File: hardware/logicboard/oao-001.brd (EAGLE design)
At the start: 47 x 47 mm, 13 parts, among them K1 G5V1, T1 2SC1815

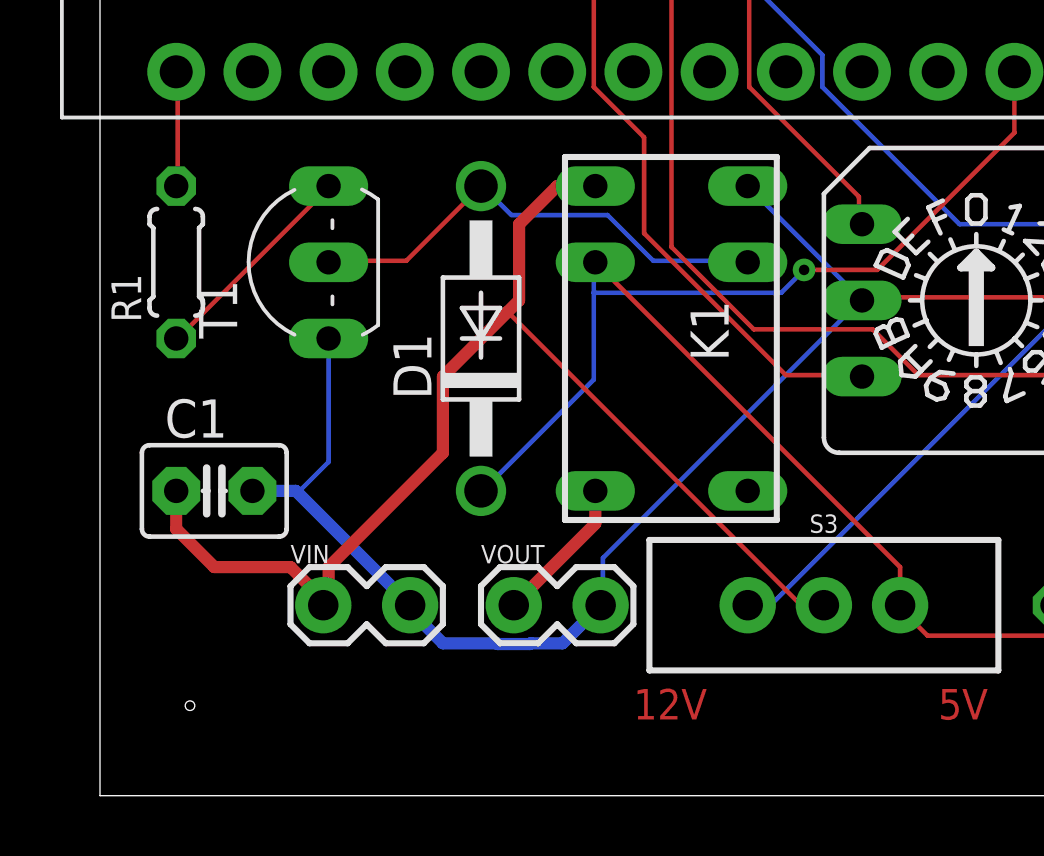
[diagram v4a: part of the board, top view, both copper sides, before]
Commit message: Changed layout.
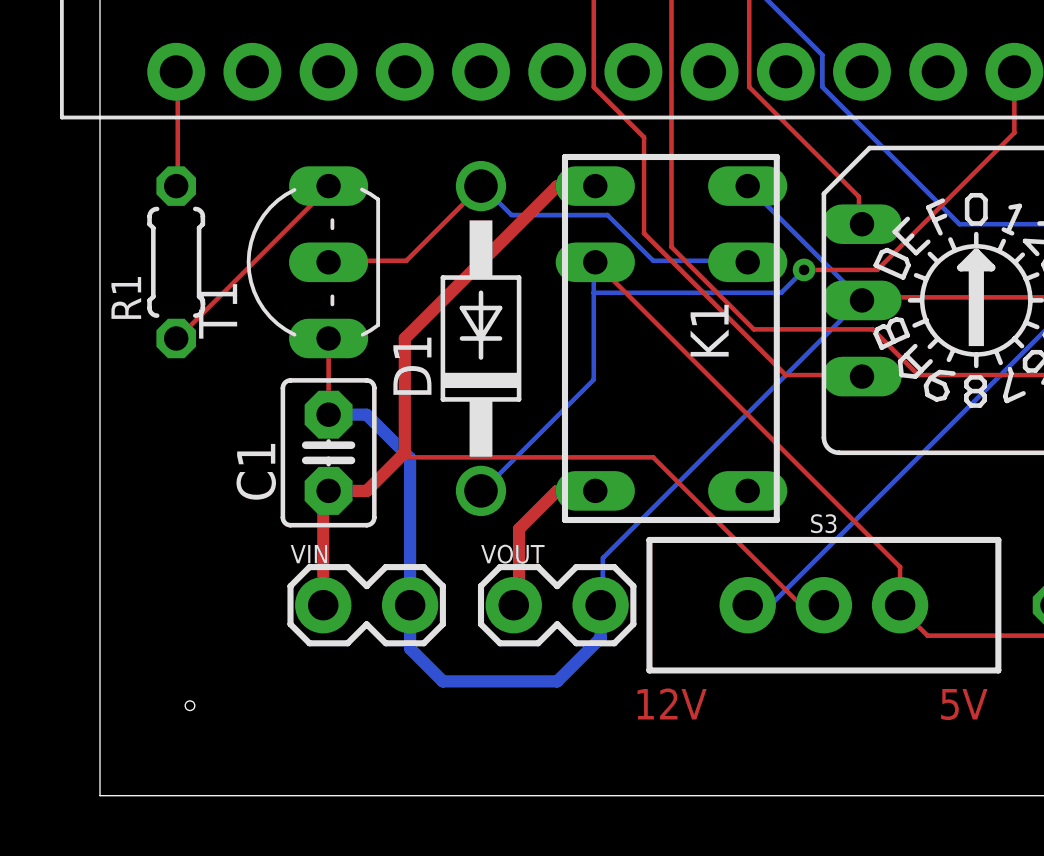
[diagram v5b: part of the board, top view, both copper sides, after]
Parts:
- moved C1 4.02 mm to (7.62, 11.4), turned to 90 degrees
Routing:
- net VDD: track 41.2 -> 35.3 mm
- net GND: track 60.1 -> 60.9 mm
- net N$1: track 4.94 -> 5.68 mm
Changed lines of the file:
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@@
 <attribute name="SF_SKU" value="COM-00102" x="24.13" y="6.35" size="1.778" layer="27" rot="R270" display="off"/>
 </element>
-<element name="C1" library="capacitor-wima" library_urn="urn:adsk.eagle:library:116" package="C2.5-3" package3d_urn="urn:adsk.eagle:package:5436/1" value="" x="3.81" y="10.16"/>
+<element name="C1" library="capacitor-wima" library_urn="urn:adsk.eagle:library:116" package="C2.5-3" package3d_urn="urn:adsk.eagle:package:5436/1" value="" x="7.62" y="11.43" rot="R90"/>
 </elements>
 <signals>
@@
 <contactref element="S3" pad="2"/>
 <contactref element="C1" pad="1"/>
+<wire x1="7.4422" y1="6.35" x2="7.4422" y2="9.9822" width="0.4064" layer="1"/>
+<wire x1="7.4422" y1="9.9822" x2="7.62" y2="10.16" width="0.4064" layer="1"/>
 <wire x1="16.51" y1="20.32" x2="15.24" y2="20.32" width="0.4064" layer="1"/>
-<wire x1="15.24" y1="20.32" x2="13.97" y2="19.05" width="0.4064" layer="1"/>
-<wire x1="13.97" y1="19.05" x2="13.97" y2="16.51" width="0.4064" layer="1"/>
-<wire x1="13.97" y1="16.51" x2="13.589" y2="16.129" width="0.4064" layer="1"/>
-<wire x1="13.589" y1="16.129" x2="11.43" y2="13.97" width="0.4064" layer="1"/>
-<wire x1="11.43" y1="13.97" x2="11.43" y2="11.43" width="0.4064" layer="1"/>
-<wire x1="11.43" y1="11.43" x2="7.62" y2="7.62" width="0.4064" layer="1"/>
-<wire x1="7.62" y1="7.62" x2="7.62" y2="6.5278" width="0.4064" layer="1"/>
-<wire x1="7.4422" y1="6.35" x2="7.62" y2="6.5278" width="0.4064" layer="1"/>
-<wire x1="2.54" y1="10.16" x2="2.54" y2="8.89" width="0.4064" layer="1"/>
-<wire x1="2.54" y1="8.89" x2="3.81" y2="7.62" width="0.4064" layer="1"/>
-<wire x1="3.81" y1="7.62" x2="6.35" y2="7.62" width="0.4064" layer="1"/>
-<wire x1="6.35" y1="7.62" x2="7.4422" y2="6.5278" width="0.4064" layer="1"/>
-<wire x1="7.4422" y1="6.5278" x2="7.4422" y2="6.35" width="0.4064" layer="1"/>
+<wire x1="15.24" y1="20.32" x2="10.16" y2="15.24" width="0.4064" layer="1"/>
+<wire x1="10.16" y1="15.24" x2="10.16" y2="11.43" width="0.4064" layer="1"/>
+<wire x1="10.16" y1="11.43" x2="10.1092" y2="11.3792" width="0.4064" layer="1"/>
+<wire x1="10.1092" y1="11.3792" x2="8.89" y2="10.16" width="0.4064" layer="1"/>
+<wire x1="8.89" y1="10.16" x2="7.62" y2="10.16" width="0.4064" layer="1"/>
 <wire x1="23.3172" y1="6.4008" x2="24.0792" y2="6.4008" width="0.1524" layer="1"/>
+<wire x1="18.4404" y1="11.2776" x2="23.3172" y2="6.4008" width="0.1524" layer="1"/>
+<wire x1="10.2108" y1="11.2776" x2="18.4404" y2="11.2776" width="0.1524" layer="1"/>
 <wire x1="24.0792" y1="6.4008" x2="24.13" y2="6.35" width="0.1524" layer="1"/>
-<wire x1="13.589" y1="16.129" x2="23.3172" y2="6.4008" width="0.1524" layer="1"/>
-<wire x1="23.3172" y1="6.4008" x2="24.13" y2="6.35" width="0.1524" layer="1"/>
+<wire x1="10.2108" y1="11.2776" x2="10.1092" y2="11.3792" width="0.1524" layer="1"/>
 </signal>
 <signal name="GND">
@@
 <contactref element="VIN" pad="2"/>
 <contactref element="C1" pad="2"/>
-<wire x1="16.6878" y1="6.35" x2="15.4178" y2="5.08" width="0.4064" layer="16"/>
-<wire x1="14.354175" y1="5.08" x2="14.328775" y2="5.0546" width="0.4064" layer="16"/>
-<wire x1="14.328775" y1="5.0546" x2="13.255625" y2="5.0546" width="0.4064" layer="16"/>
-<wire x1="13.255625" y1="5.0546" x2="13.230225" y2="5.08" width="0.4064" layer="16"/>
-<wire x1="13.230225" y1="5.08" x2="11.43" y2="5.08" width="0.4064" layer="16"/>
-<wire x1="15.4178" y1="5.08" x2="14.354175" y2="5.08" width="0.4064" layer="16"/>
-<wire x1="11.43" y1="5.08" x2="10.3378" y2="6.1722" width="0.4064" layer="16"/>
-<wire x1="10.3378" y1="6.1722" x2="10.3378" y2="6.35" width="0.4064" layer="16"/>
-<wire x1="10.3378" y1="6.35" x2="6.5278" y2="10.16" width="0.4064" layer="16"/>
-<wire x1="6.5278" y1="10.16" x2="5.08" y2="10.16" width="0.4064" layer="16"/>
+<wire x1="10.3378" y1="6.35" x2="10.3378" y2="4.9022" width="0.4064" layer="16"/>
+<wire x1="10.3378" y1="4.9022" x2="11.43" y2="3.81" width="0.4064" layer="16"/>
+<wire x1="11.43" y1="3.81" x2="15.24" y2="3.81" width="0.4064" layer="16"/>
+<wire x1="16.6878" y1="5.2578" x2="16.6878" y2="6.35" width="0.4064" layer="16"/>
+<wire x1="15.24" y1="3.81" x2="16.6878" y2="5.2578" width="0.4064" layer="16"/>
+<wire x1="7.62" y1="12.7" x2="8.89" y2="12.7" width="0.4064" layer="16"/>
+<wire x1="10.3378" y1="11.2522" x2="10.3378" y2="6.35" width="0.4064" layer="16"/>
+<wire x1="8.89" y1="12.7" x2="10.3378" y2="11.2522" width="0.4064" layer="16"/>
 <wire x1="36.8808" y1="17.0688" x2="36.8808" y2="16.6116" width="0.1524" layer="1"/>
 <wire x1="38.4048" y1="18.5928" x2="36.8808" y2="17.0688" width="0.1524" layer="1"/>
@@
 <wire x1="36.8808" y1="16.6116" x2="36.83" y2="16.51" width="0.1524" layer="1"/>
 <wire x1="35.6616" y1="24.0792" x2="35.56" y2="24.13" width="0.1524" layer="1"/>
-<wire x1="7.62" y1="11.1252" x2="7.62" y2="15.24" width="0.1524" layer="16"/>
-<wire x1="6.7056" y1="10.2108" x2="7.62" y2="11.1252" width="0.1524" layer="16"/>
-<wire x1="6.7056" y1="10.2108" x2="6.5278" y2="10.16" width="0.1524" layer="16"/>
-<wire x1="25.4" y1="16.51" x2="21.59" y2="20.32" width="0.1524" layer="16"/>
+<wire x1="7.62" y1="12.7" x2="7.62" y2="15.24" width="0.1524" layer="1"/>
+<wire x1="21.59" y1="20.32" x2="25.4" y2="16.51" width="0.1524" layer="16"/>
 <wire x1="16.764" y1="7.9248" x2="16.764" y2="6.4008" width="0.1524" layer="16"/>
 <wire x1="25.2984" y1="16.4592" x2="16.764" y2="7.9248" width="0.1524" layer="16"/>
@@
 <contactref element="K1" pad="5"/>
 <contactref element="VOUT" pad="1"/>
-<wire x1="13.7922" y1="6.35" x2="16.51" y2="9.0678" width="0.4064" layer="1"/>
-<wire x1="16.51" y1="9.0678" x2="16.51" y2="10.16" width="0.4064" layer="1"/>
+<wire x1="16.51" y1="10.16" x2="15.24" y2="10.16" width="0.4064" layer="1"/>
+<wire x1="15.24" y1="10.16" x2="13.97" y2="8.89" width="0.4064" layer="1"/>
+<wire x1="13.97" y1="8.89" x2="13.97" y2="6.5278" width="0.4064" layer="1"/>
+<wire x1="13.97" y1="6.5278" x2="13.7922" y2="6.35" width="0.4064" layer="1"/>
 </signal>
 <signal name="N$2">
@@
 <contactref element="R2" pad="1"/>
 <wire x1="31.8516" y1="7.0104" x2="31.8516" y2="6.4008" width="0.1524" layer="16"/>
-<wire x1="31.8516" y1="6.4008" x2="31.75" y2="6.35" width="0.1524" layer="16"/>
 <wire x1="39.3192" y1="14.478" x2="31.8516" y2="7.0104" width="0.1524" layer="16"/>
 <wire x1="39.3192" y1="28.0416" x2="39.3192" y2="14.478" width="0.1524" layer="16"/>
 <wire x1="28.0416" y1="39.3192" x2="39.3192" y2="28.0416" width="0.1524" layer="16"/>
+<wire x1="31.8516" y1="6.4008" x2="31.75" y2="6.35" width="0.1524" layer="16"/>
 <wire x1="28.0416" y1="39.3192" x2="27.94" y2="39.37" width="0.1524" layer="16"/>
 </signal>

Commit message: GND.
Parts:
- VOLTAGE-SELECT: value NC: 5V, NO: 12V -> 12V-5V
- moved D1 1.27 mm to (12.7, 16.5)
- moved VOUT 1.27 mm to (12.7, 6.35)
- moved C1 1.27 mm to (7.62, 12.7)
- moved R1 1.27 mm to (2.54, 19.1)
- moved T1 1.27 mm to (7.62, 19.1)
- renumbered D2 to LED, K1 to RELAY, S1 to ON-INT, S2 to OFF-INT, S3 to VOLTAGE-SELECT
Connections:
- net N$13 renamed LEDDRIVE
- net N$15 renamed V12
- net N$2 renamed RELAYDRIVE
- removed net N$12: OFF-INT.1, U$1.P$9
- new net N$2: OFF-INT.8, U$1.P$5
- net N$11: now also OFF-INT.1; no longer OFF-INT.2
- net N$5: now also OFF-INT.4; no longer OFF-INT.8
- net N$6: now also OFF-INT.2; no longer OFF-INT.4
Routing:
- net N$2: track 0.00 -> 45.4 mm
- net N$12: track 26.2 -> 0.00 mm
- net N$11: track 42.0 -> 31.8 mm
- net N$9: track 41.6 -> 50.3 mm
- net LEDDRIVE: track 40.9 -> 34.6 mm
- net N$5: track 41.2 -> 35.1 mm, vias 0 -> 1
- net VCC: track 59.3 -> 64.3 mm, vias 1 -> 0
- net N$6: track 40.0 -> 43.7 mm
- net N$7: track 39.5 -> 41.3 mm
- net RELAYDRIVE: track 3.84 -> 2.58 mm
- net GND: track 60.9 -> 61.6 mm
- net N$4: track 16.1 -> 16.6 mm
- added copper zone on layer 1, net GND
- added copper zone on layer 16, net GND
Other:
- board text added: "GEYSER 1.0 by Pineapple Computer"
- board text added: "VIN=12V -> Connect L&C; VIN=5V -> Connect C&R."
- board text removed: "12V"
- board text removed: "5V"
- board text removed: "ON-AND-OFF Rev. 1 by Pineapple.cc"
